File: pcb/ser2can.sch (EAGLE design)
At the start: 67 parts, among them Q1 8MHz, Q2 32768Hz, SW1 KSS-2EG4430, X1 MSTBA4

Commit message: sch&pcb some modifications
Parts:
- removed SW1: KSS-2EG4430, buttons:KSS-2EG4430
- removed X3: (no value), pinhead-fixdrills:PINHD-1X5_2.00
- added JP3: (no value), pinhead-fixdrills:PINHD-1X2_2.54S
- added SWD: SWD-6, jtag:SWD-6
- JP2: device pinhead-fixdrills:PINHD-1X2_2.00 -> pinhead-fixdrills:PINHD-1X2_2.54S
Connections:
- new net PA15: DD2.JTDI/(TIM2_CH1_ETR/PA15/SPI1_NSS), X2.20
- net !RESET: now also SWD.5; no longer SW1.S, X3.4
- net +3V3: now also SWD.1; no longer X3.1
- net CAN_L: now also JP3.1
- net CAN_L_R: now also JP3.2
- net GND: now also SWD.3; no longer SW1.P, X2.20, X3.5
- net SWCLK: now also SWD.2; no longer X3.3
- net SWDIO: now also SWD.4; no longer X3.2
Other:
- note added: "Terminator"
- note removed: "SWD"
- note removed: "reset"
- moved on the sheet: C1, C2, C6, C7, C8, C9, D1, DA1, DA1', DA2, F1, F2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

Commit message: little changes. pictures
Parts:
- removed JP3: (no value), pinhead-fixdrills:PINHD-1X2_2.54S
- added C23: 100uF/6.3V, rc-master-smd:CP_SMCC
- added R21: 330, rc-master-smd:R_0603
- added SW1: KSS-2EG4430, buttons:KSS-2EG4430
- C1: value 560pF -> 10uF
- C10: value 0.1 -> 22pF
- C11, C12: value 22pF -> 0.1
- C15: value 0.1 -> (none); device rc-master-smd:C_0603 -> rc-master:C_C050-110X055
- C17: value 0.1 -> 100uF/6.3V; device rc-master-smd:C_0805 -> rc-master-smd:CP_SMCC
- C18: device rc-master-smd:C_0805 -> rc-master-smd:C_0603
- C19: value 100uF/6.3V -> 560pF; device rc-master-smd:CP_SMCC -> rc-master-smd:C_0603
- C2: value 560pF -> 10pF
- C20: value 0.1 -> 560pF
- C21, C22: value 10pF -> 0.1; device rc-master-smd:C_0603 -> rc-master-smd:C_0805
- C3: value 10uF -> 0.1
- C5: value 0.1 -> 10pF
- C6: value 0.1 -> NC (0.1)
- C7: value 0.1 -> 0.1 (NC)
- C8: value 100uF/6.3V -> 22pF; device rc-master-smd:CP_SMCC -> rc-master-smd:C_0603
- C9: value (none) -> 0.1; device rc-master:C_C050-110X055 -> rc-master-smd:C_0603
- JP2: device pinhead-fixdrills:PINHD-1X2_2.54S -> pinhead-fixdrills:PINHD-1X2_2.00
- Q1: value 8MHz -> 32768Hz; device discrete:CRYSTAL-HC49S -> discrete:CRYSTAL-MM20SS
- Q2: value 32768Hz -> 8MHz; device discrete:CRYSTAL-MM20SS -> discrete:CRYSTAL-HC49S
- R1: value NC -> 1K
- R10: value 1M -> 330
- R11: value 10 -> 330
- R12: value 330 -> 10K
- R13: value 330 -> NC
- R14: value 10K -> 330
- R15: value 330 -> 0
- R16, R17: value 4.7K -> 100
- R18: value 10K -> 4.7K
- R19: value 1K -> 4.7K
- R2, R3: value 100 -> 10K
- R20: value 1M -> 120; device rc-master-smd:R_0603 -> rc-master-smd:R_0805
- R4: value 120 -> 1M; device rc-master-smd:R_0805 -> rc-master-smd:R_0603
- R5: value 0 -> 1M
- R6: value 330 -> 0/FB
- R7: value nc -> 10K; device rc-master-smd:R_1206 -> rc-master-smd:R_0603
- R8: value 1M -> nc
- R9: value 10K -> 1M; device rc-master-smd:R_0603 -> rc-master-smd:R_1206
- X1: value MSTBA4 -> (none); device con-phoenix-508:MSTBA4 -> pinhead-fixdrills:PINHD-2X10_2.54
- X2: value (none) -> MSTBA4; device pinhead-fixdrills:PINHD-2X10_2.54 -> con-phoenix-508:MSTBA4
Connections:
- removed net N$11: DD2.PC13/TAMPER-RTC
- new net PC13: DD2.PC13/TAMPER-RTC, R3.2
- net !LCD_CS: now also X1.13; no longer X2.13
- net !RESET: now also C6.2, C7.1, R7.1; no longer C10.2, R9.1
- net +3V3: now also C11.1, C13.1, C22.1, C23.+, C9.1, R18.2, R19.2, R21.2, R6.1, R7.2, SW1.P, X1.1; no longer C14.1, C15.1, C16.1, C19.+, C20.1, JP2.1, R11.1, R15.2, R16.2, R17.2, R9.2, X2.1
- net +5V: now also C1.1, C14.1, C21.1, R8.1; no longer C17.1, C4.1, C6.1, R7.1
- net BOOT0: now also R2.2; no longer R18.2
- net BOOT1: now also R11.1, R12.1; no longer R13.1, R14.1
- net CANH: now also R16.2; no longer R2.2
- net CANL: now also R17.2; no longer R3.2
- net CAN_H: now also R20.1, X2-3.1; no longer R4.1, X1-3.1
- net CAN_L: now also JP1.1, X2-2.1; no longer JP3.1, X1-2.1
- net CAN_L_R: now also JP1.2, R20.2, X2-1.1; no longer JP3.2, R4.2, X1-1.1
- net DTR: now also C6.1; no longer C10.1
- net GND: now also C1.2, C10.2, C2.2, C23.-, C7.2, C8.2, JP2.1, LED1.C, R1.1, R12.2, R9.1, X1.19; no longer C16.2, C17.2, C19.-, C20.2, C6.2, JP1.1, LED3.C, R14.2, R19.1, R8.1, X2.19
- net ISOGND: now also C15.1, C16.2, C17.-, C19.2, C20.2, LED3.C, R15.2, R9.2, X2-4.1; no longer C1.2, C2.2, C7.2, C8.-, C9.1, LED1.C, R5.2, R8.2, X1-4.1
- net ISOVCC: now also C16.1, C17.+, R13.2, R14.1, R8.2; no longer C7.1, C8.+, R1.2, R6.1, R7.2
- net LCD_CK: now also X1.14; no longer X2.14
- net LCD_SI: now also X1.12; no longer X2.12
- net N$10: now also R10.1; no longer R12.1
- net N$15: now also R13.1, R15.1; no longer R1.1, R5.1
- net N$16: now also C4.1; no longer C5.1
- net N$2: now also R1.2, R2.1, R3.1, SW1.S; no longer JP2.2, R18.1, R19.2
- net N$4: now also LED2.A, R11.2; no longer LED3.A, R13.2
- net N$5: now also LED1.A, R10.2; no longer LED2.A, R12.2
- net N$54: now also C20.1, R17.1; no longer C2.1, R3.1
- net N$55: now also C19.1, R16.1; no longer C1.1, R2.1
- net N$6: now also LED3.A, R14.2; no longer LED1.A, R6.2
- net N$9: now also R21.1; no longer R15.1
- net OSC_IN: now also C8.1, Q2.1, R5.1; no longer C11.1, Q1.1, R10.1
- net OSC_IN1: now also C5.1, Q1.2, R4.2; no longer C22.1, Q2.2, R20.2
- net OSC_OUT: now also C10.1, Q2.2, R5.2; no longer C12.1, Q1.2, R10.2
- net OSC_OUT1: now also C2.1, Q1.1, R4.1; no longer C21.1, Q2.1, R20.1
- net PA0: now also X1.3; no longer X2.3
- net PA1: now also X1.4; no longer X2.4
- net PA15: now also X1.20; no longer X2.20
- net PA2: now also X1.5; no longer X2.5
- net PA3: now also X1.6; no longer X2.6
- net PA4: now also X1.7; no longer X2.7
- net PA5: now also X1.8; no longer X2.8
- net PA6: now also X1.9; no longer X2.9
- net PA7: now also X1.10; no longer X2.10
- net PB0: now also X1.11; no longer X2.11
- net PB13: now also X1.15; no longer X2.15
- net PB14: now also X1.16; no longer X2.16
- net PB15: now also X1.17; no longer X2.17
- net PB3: now also X1.18; no longer X2.18
- net SCL1: now also R18.1; no longer R16.1
- net SDA1: now also R19.1; no longer R17.1
- net VBAT: now also JP2.2, X1.2; no longer JP1.2, X2.2
- net VDDA: now also C12.1, R6.2; no longer C13.1, R11.2
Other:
- note removed: "Extensions"

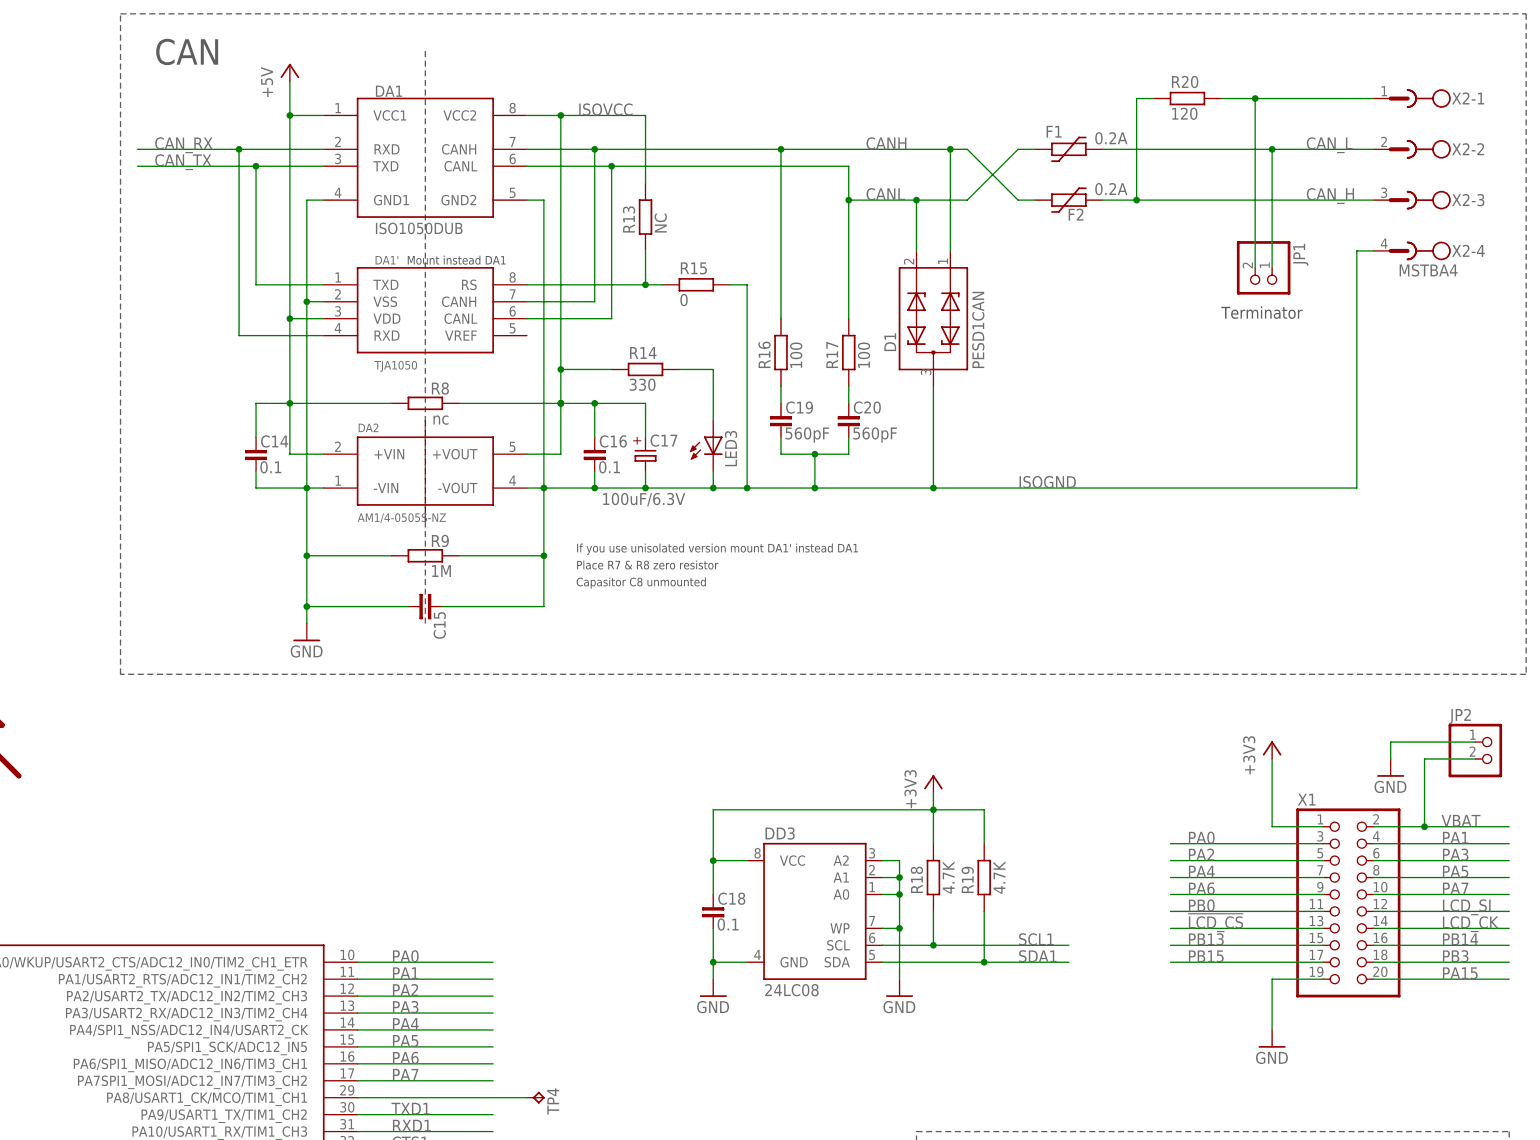
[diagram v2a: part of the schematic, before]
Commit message: Add alternative DC-DC B0505S-1W (MornSun, etc)
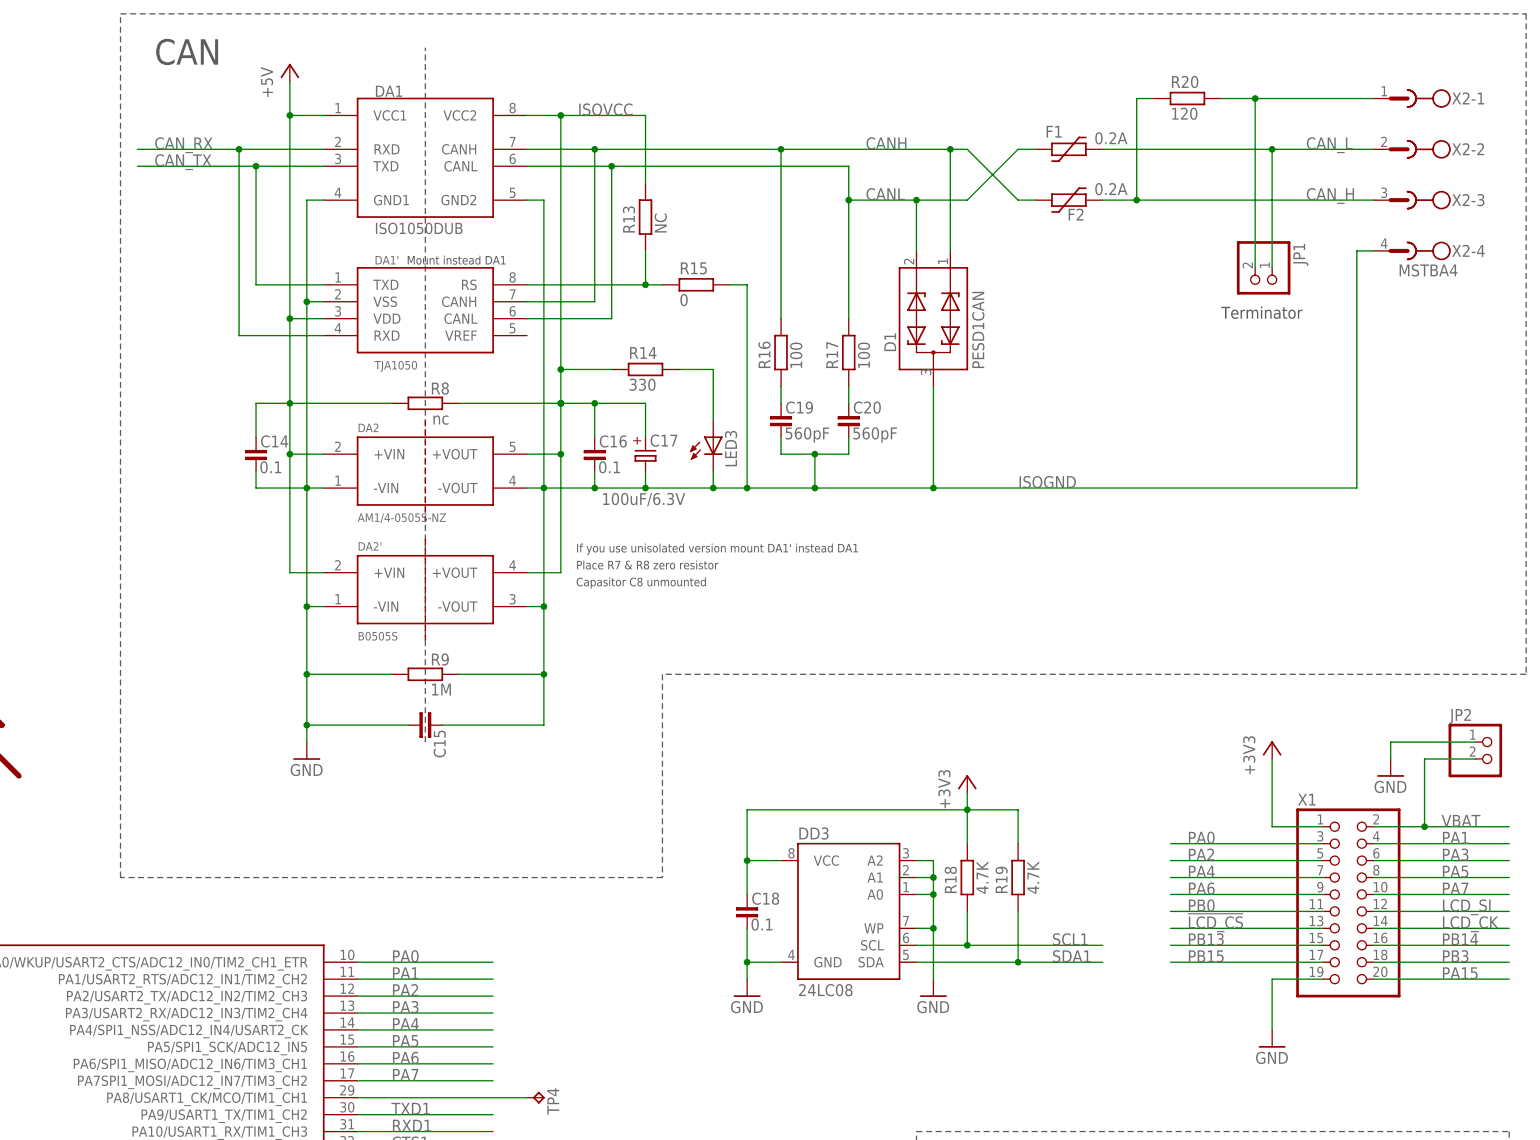
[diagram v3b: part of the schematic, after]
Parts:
- added DA2': B0505S, dcdc-isolated:VA-S1
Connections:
- net +5V: now also DA2'.+VIN
- net GND: now also DA2'.-VIN
- net ISOGND: now also DA2'.-VOUT
- net ISOVCC: now also DA2'.+VOUT
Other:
- moved on the sheet: C15, C18, DD3, R18, R19, R9
